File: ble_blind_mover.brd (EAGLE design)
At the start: 160 x 100 mm, 52 parts, among them J1 105017-0001, Q1 DMG6968U-7, Q2 DMG6968U-7, U1 MIC5205-3.3YM5-TR, U2 YJ-14015, U3 VIPER012LS

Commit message: Brd routed, clearance adjustment still WIP
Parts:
- removed C12: 470pF, rcl:C0603
- removed C15: 100uF, resistor:CT7343
- removed S1, S2: (no value), switch-omron:B3F-31XX
- removed U1: MIC5205-3.3YM5-TR, LTC_By_element14_Batch_1:SOT95P280X145-5N
- added C16, C17: 1uF, rcl:C0603
- added C18: 470pF, rcl:C0603
- added D6: STTH1L06A, xCommonLib:DO214AC
- added J2: (no value), tag-connect:TC2030-MCP-NL
- added R15: 0, rcl:0207/7
- added U4: MIC5205-3.3YM5-TR, LTC_By_element14_Batch_1:SOT95P280X145-5N
- C11: value 1uF -> 100uF; device rcl:C0603 -> rcl:C1812
- R9: device rcl:R0603 -> rcl:R1206
- moved S4 155.7 mm to (45.0, 55.0)
- moved S3 154.6 mm to (54.1, 55.0), turned to 90 degrees
- moved R11 142.7 mm to (53.6, 21.6), turned to 270 degrees
- moved C11 134.8 mm to (31.2, 10.7), turned to 90 degrees
- moved R9 129.3 mm to (34.3, 10.7), turned to 270 degrees
- moved R13 124.1 mm to (51.6, 21.6), turned to 90 degrees
- moved J1 117.3 mm to (10.9, 1.52)
- moved C10 109.8 mm to (24.6, 1.78), turned to 180 degrees
- moved C3 102.0 mm to (11.7, 48.0), turned to 90 degrees
- moved C1 99.0 mm to (7.62, 48.0), turned to 90 degrees
- moved SWD 97.5 mm to (34.3, 47.5)
- moved D2 91.2 mm to (36.8, 56.1), turned to 270 degrees
- moved R12 85.0 mm to (32.8, 57.1), turned to 180 degrees
- moved R4 79.6 mm to (5.59, 48.0), turned to 270 degrees
- moved R10 79.5 mm to (32.8, 59.2), turned to 180 degrees
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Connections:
- removed net N$11: C12.1, U1.4
- removed net VIPER_GND: C13.2, C7.2, D3.C, L1.1, U3.1, U3.3
- new net +5V: C10.1, C11.1, C16.1, D4.A, D6.C, L1.2, R9.2, U4.1, U4.3
- new net HOT_GND: C13.2, C14.2, C4.2, C5.2, C6.2, C7.2, D3.C, L1.1, R13.1, R15.2, U3.1, U3.3
- new net N$1: C18.1, U4.4
- net +3V3: now also C17.1, J2.1, U4.5; no longer C11.1, C15.+, D4.A, L1.2, R9.2, U1.5
- net BTN_DOWN: now also S4.1, S4.2; no longer S1.2
- net BTN_UP: no longer S2.2
- net GND: now also C16.2, C17.2, C18.2, J2.5, R15.1, U4.2; no longer C11.2, C12.2, S1.1, S2.1, U1.2
- net LED_B: now also U2.P.18; no longer U2.P.19
- net LED_G: now also U2.P.19; no longer U2.P.18
- net NEUTRAL: now also C11.2; no longer C14.2, C15.-, C4.2, C5.2, C6.2, R13.1
- net SWDCLK: now also J2.4
- net SWDIO: now also J2.2
- net VUSB: now also D6.A; no longer C10.1, U1.1, U1.3
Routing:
- net GND: track 0.00 -> 212.9 mm, vias 0 -> 4
- net +3V3: track 6.14 -> 146.5 mm, vias 0 -> 2
- net HOT_GND: track 0.00 -> 60.3 mm
- net +5V: track 0.00 -> 56.1 mm
- net BTN_UP: track 0.00 -> 41.0 mm, vias 0 -> 2
- net GO_DOWN: track 0.00 -> 32.0 mm
- net RELAY_COIL_UP: track 0.00 -> 31.9 mm, vias 0 -> 3
- net BTN_DOWN: track 0.00 -> 28.1 mm, vias 0 -> 1
- net NEUTRAL: track 96.6 -> 123.9 mm
- net GO_UP: track 0.00 -> 22.6 mm, vias 0 -> 2
- net VIPER_FB: track 1.97 -> 21.2 mm
- net LINE_FILTERED: track 10.9 -> 27.5 mm, vias 0 -> 1
- net VIPER_GND: track 16.4 -> 0.00 mm
- net SWDIO: track 0.00 -> 15.3 mm, vias 0 -> 1
- net SWDCLK: track 0.00 -> 15.0 mm, vias 0 -> 1
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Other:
- board size 160 x 100 mm -> 62 x 60.5 mm

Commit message: Fixed board eouting for increased low/high voltage clearance
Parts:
- removed R15: 0, rcl:0207/7
- added R16: 0, rcl:0207/7
- moved R9 4.74 mm to (35.8, 6.17)
- moved C11 4.74 mm to (32.7, 6.17)
- moved D3 4.51 mm to (32.7, 12.5)
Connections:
- removed net HOT_GND: C13.2, C14.2, C4.2, C5.2, C6.2, C7.2, D3.C, L1.1, R13.1, R15.2, U3.1, U3.3
- new net NEUTRAL_DISCONNECTABLE: C11.2, D3.A, R16.2, R9.1
- net GND: now also C13.2, C14.2, C4.2, C5.2, C6.2, C7.2, D3.C, L1.1, R13.1, U3.1, U3.3; no longer R15.1
- net NEUTRAL: now also R16.1; no longer C11.2, D3.A, R9.1
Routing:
- net HOT_GND: track 60.3 -> 0.00 mm
- net GND: track 212.9 -> 270.3 mm, vias 4 -> 5
- net NEUTRAL: track 123.9 -> 95.2 mm
- net NEUTRAL_DISCONNECTABLE: track 0.00 -> 24.2 mm
- net LINE_FILTERED: track 27.5 -> 32.1 mm
- net +5V: track 56.1 -> 54.5 mm
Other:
- outline, holes or cut-outs redrawn

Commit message: Added power connecting pinheads
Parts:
- added JP1, JP2: (no value), pinhead:1X02
- moved FUSE_MAINS 2.00 mm to (47.2, 35.8)
- moved D4 1.58 mm to (55.1, 15.0)
- moved D5 1.58 mm to (50.3, 15.0)
- moved C14 1.58 mm to (44.5, 17.0)
- moved C4 1.58 mm to (51.6, 17.6)
- moved C5 1.58 mm to (47.0, 18.3)
- moved C6 1.58 mm to (49.0, 18.3)
- moved L1 1.58 mm to (44.0, 6.88)
- moved R11 1.58 mm to (53.1, 20.1)
- moved R13 1.58 mm to (51.1, 20.1)
- moved R14 1.58 mm to (47.8, 20.9)
- moved C13 1.58 mm to (44.0, 14.5)
- moved C7 1.58 mm to (46.0, 14.5)
- moved U3 1.58 mm to (39.1, 15.8)
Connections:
- net NEUTRAL_DISCONNECTABLE renamed NEUTRAL_SEP
- net +3V3: now also JP1.1
- net +5V: now also JP2.1
- net GND: now also JP1.2, JP2.2
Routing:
- net +5V: track 54.5 -> 66.6 mm, vias 0 -> 2
- net LINE_UNFUSED: track 15.9 -> 13.9 mm
- net NEUTRAL_SEP: track 24.2 -> 22.5 mm
- net GND: track 270.3 -> 269.0 mm
- net LINE_FILTERED: track 32.1 -> 32.8 mm
- net NEUTRAL: track 95.2 -> 94.5 mm

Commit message: Aligned silkscreen labels
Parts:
- C1: value 10nF -> 10n
- C13, C2, C4: value 100nF -> 100n
- C18: value 470pF -> 470p
- C5: value 750pF -> 750p
- C6: value 22nF -> 22n
- C8, C9: value 120nF -> 120n
- L2: value 470uH -> 470u
- R1: value 15 -> 15R
- R10, R12, R8: value 470 -> 470R
- R16: value 0 -> 0R
- R3, R5: value 10 -> 10R
- renumbered D2 to LED1
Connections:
- net N$1 renamed U4_BYPASS
- new net SCL: U2.P.10
- new net SDA: U2.P.13
- net GO_UP: now also U2.P.12; no longer U2.P.13
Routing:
- net GO_DOWN: track 32.0 -> 31.1 mm
- net GO_UP: track 22.6 -> 23.5 mm

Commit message: Added RTC
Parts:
- added C12: 10n, rcl:C0603
- added C15: 100n, rcl:C0603
- added C19: 1uF, rcl:C0603
- added JP3: (no value), pinhead:1X02
- added R15, R17: 4K7, rcl:R0603
- added U1: MCP7940N-I/SN, MCP7940N-I_SN:SOIC127P600X175-8N
- added Y1: LFXTAL016178, LFXTAL016178:LFXTAL016178_1
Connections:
- new net RTC_XTAL1: U1.1, Y1.1
- new net RTC_XTAL2: U1.2, Y1.4
- new net VBAT: JP3.1, U1.3
- net +3V3: now also C12.1, C15.1, C19.1, R15.2, R17.2, U1.8
- net GND: now also C12.2, C15.2, C19.2, JP3.2, U1.4
- net SCL: now also R17.1, U1.6
- net SDA: now also R15.1, U1.5
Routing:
- net SCL: track 0.00 -> 23.5 mm, vias 0 -> 1
- net +3V3: track 146.9 -> 170.3 mm, vias 2 -> 3
- net SDA: track 0.00 -> 21.4 mm, vias 0 -> 1
- net GND: track 268.9 -> 282.3 mm
- net GO_DOWN: track 31.1 -> 42.1 mm
- net VBAT: track 0.00 -> 8.48 mm
- net RTC_XTAL2: track 0.00 -> 6.10 mm
- net BTN_DOWN: track 28.1 -> 25.1 mm
- net BTN_UP: track 41.0 -> 38.0 mm
- net RTC_XTAL1: track 0.00 -> 2.27 mm

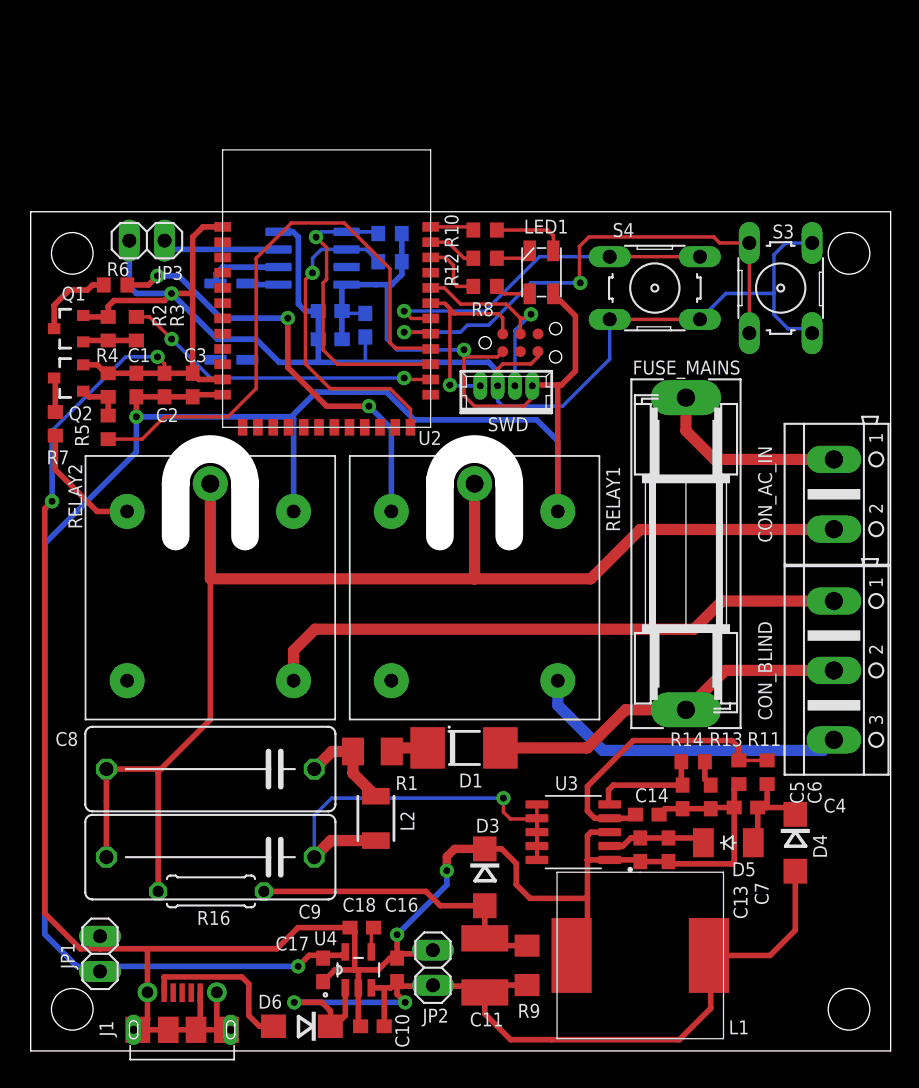
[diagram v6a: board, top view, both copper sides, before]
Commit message: - Get rid from Viper PSU in favour of a Meanwell module - Make the contours to fit in a Kradex Z21 box
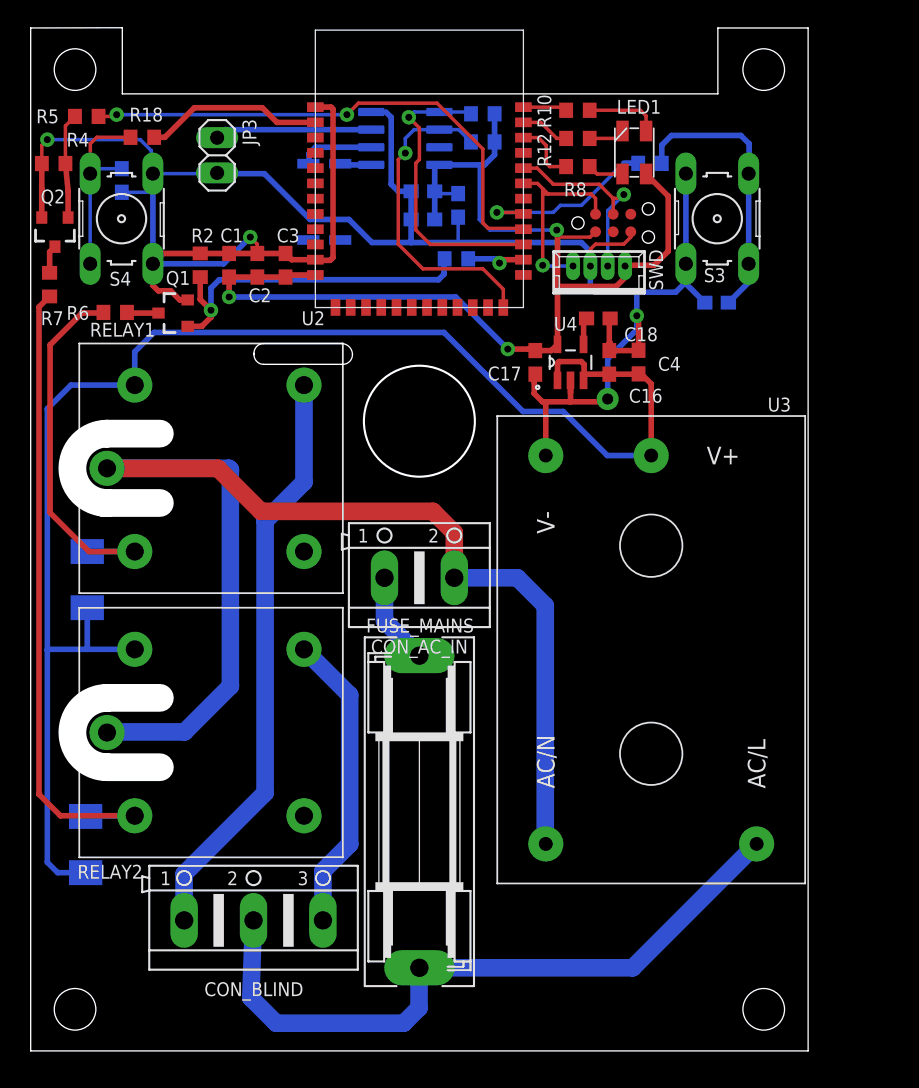
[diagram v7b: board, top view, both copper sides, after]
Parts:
- removed C10, C7: 1uF, rcl:C0603
- removed C11: 100uF, rcl:C1812
- removed C13: 100n, rcl:C0603
- removed C14: TBD, rcl:C0603
- removed C5: 750p, rcl:C0603
- removed C6: 22n, rcl:C0603
- removed C8, C9: 120n, rcl:C150-064X183
- removed D1: SM4007, _hhn_diodes_smd:MELF-MLL41_DO213AB
- removed D3, D4, D6: STTH1L06A, xCommonLib:DO214AC
- removed D5: (no value), diode_:SOD-123_MINI-SMA
- removed J1: 105017-0001, 105017-0001:MOLEX_105017-0001
- removed JP1, JP2: (no value), pinhead:1X02
- removed L1: DE1207-820, ferrocore:DE1207
- removed L2: 470u, SparkFun:1210
- removed R1: 15R, rcl:M1206
- removed R11: 82K, rcl:R0603
- removed R13: 47K, rcl:R0603
- removed R14: 100K, rcl:R0603
- removed R16: 0R, rcl:0207/7
- removed R9: 3K3, rcl:R1206
- added C20, C21: 10n, rcl:C0603
- added D2, D8: SK16, diode:DO-214AC
- added R18, R19: TBD, rcl:R0603
- RELAY1: value RM50-3011-85-1003 -> RM513021851005
- RELAY2: value RM50-3011-85-1003 -> RM51-3021-85-1005
- U3: value VIPER012LS -> IRM-01-5; device st_viper:SOIC100P600X175-10N -> meanwell_irm_v7:IRM_01/02
- moved C18 47.1 mm to (40.9, 52.8), turned to 0 degrees
- moved C16 46.4 mm to (41.7, 49.6)
- moved C17 46.4 mm to (36.4, 49.6)
- moved U4 46.4 mm to (38.9, 49.6)
- moved CON_BLIND 45.6 mm to (16.1, 9.41), turned to 0 degrees
- moved S4 38.8 mm to (6.55, 60.0), turned to 90 degrees
- moved C4 33.0 mm to (43.8, 49.7), turned to 90 degrees
- moved CON_AC_IN 30.5 mm to (28.0, 34.1), turned to 0 degrees
- moved FUSE_MAINS 26.7 mm to (28.0, 17.2)
- moved RELAY1 26.5 mm to (5.51, 42.0), turned to 0 degrees
- moved R3 23.6 mm to (30.7, 57.1), flipped to the bottom, turned to 0 degrees
- moved R5 22.5 mm to (4.04, 67.4), turned to 0 degrees
- moved RELAY2 19.4 mm to (5.51, 23.0), turned to 0 degrees
- moved R4 16.4 mm to (1.66, 64.0), turned to 0 degrees
- moved U3 14.3 mm to (44.7, 28.9), turned to 90 degrees
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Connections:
- removed net BLIND_DOWN: CON_BLIND.1, RELAY2.14
- removed net BLIND_UP: CON_BLIND.3, RELAY1.14
- removed net LINE_FILTERED: C9.1, L2.2, U3.10, U3.6, U3.7, U3.8, U3.9
- removed net LINE_RECTIFIED: D1.C, R1.1
- removed net LINE_RECTIFIED_R: C8.1, L2.1, R1.2
- removed net NEUTRAL_SEP: C11.2, D3.A, R16.2, R9.1
- removed net VIPER_COMP: C5.1, R14.2, U3.5
- removed net VIPER_COMP_MID: C6.1, R14.1
- removed net VIPER_FB: C14.1, R11.1, R13.2, U3.4
- removed net VIPER_PRE_FB: C4.1, D4.C, D5.A, R11.2
- removed net VIPER_VCC: C13.1, C7.1, D5.C, U3.2
- removed net VUSB: D6.A, J1.1
- new net BLIND_DOWN_AC: CON_BLIND.3, RELAY2.14
- new net BLIND_UP_AC: CON_BLIND.1, RELAY1.14
- new net BTN_DOWN_R: C20.1, R18.1, S4.1, S4.2
- new net BTN_UP_R: C21.1, R19.1, S3.1, S3.2
- net +3V3: no longer JP1.1, RELAY1.A1, RELAY2.A1
- net +5V: now also C4.1, D2.C, D8.C, RELAY1.A1, RELAY2.A1, U3.V+; no longer C10.1, C11.1, D4.A, D6.C, JP2.1, L1.2, R9.2
- net BTN_DOWN: now also R18.2, U2.P.21; no longer S4.1, S4.2, U2.P.16
- net BTN_UP: now also R19.2; no longer S3.1, S3.2
- net GND: now also C20.2, C21.2, U3.V-; no longer C10.2, C13.2, C14.2, C5.2, C6.2, C7.2, D3.C, J1.5, J1.MH1, J1.MH2, J1.MH3, J1.MH4, J1.P$10, J1.P$11, J1.P$8, J1.P$9, JP1.2, JP2.2, L1.1, R13.1, U3.1, U3.3
- net LINE_FUSED: now also U3.AC/L; no longer D1.A
- net NEUTRAL: now also U3.AC/N; no longer C8.2, C9.2, R16.1
- net RELAY_COIL_DOWN: now also D8.A
- net RELAY_COIL_UP: now also D2.A
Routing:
- net GND: track 282.3 -> 166.7 mm, vias 5 -> 4
- net +3V3: track 170.3 -> 86.6 mm
- net +5V: track 66.6 -> 111.0 mm, vias 2 -> 0
- net BLIND_DOWN: track 42.6 -> 0.00 mm
- net BLIND_UP_AC: track 0.00 -> 42.2 mm
- net RELAY_COIL_DOWN: track 8.88 -> 47.3 mm
- net LINE_FILTERED: track 32.8 -> 0.00 mm, vias 1 -> 0
- net BTN_UP: track 38.0 -> 13.6 mm, vias 2 -> 1
- net LINE_FUSED: track 26.4 -> 49.8 mm
- net BLIND_UP: track 23.3 -> 0.00 mm
- net NEUTRAL_SEP: track 22.5 -> 0.00 mm
- net BLIND_DOWN_AC: track 0.00 -> 21.7 mm
- net MOTOR_A_GATE_R: track 3.87 -> 25.1 mm, vias 0 -> 1
- net VIPER_FB: track 21.2 -> 0.00 mm
- net BTN_UP_R: track 0.00 -> 20.3 mm
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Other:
- board size 62 x 60.5 mm -> 56 x 73.8 mm

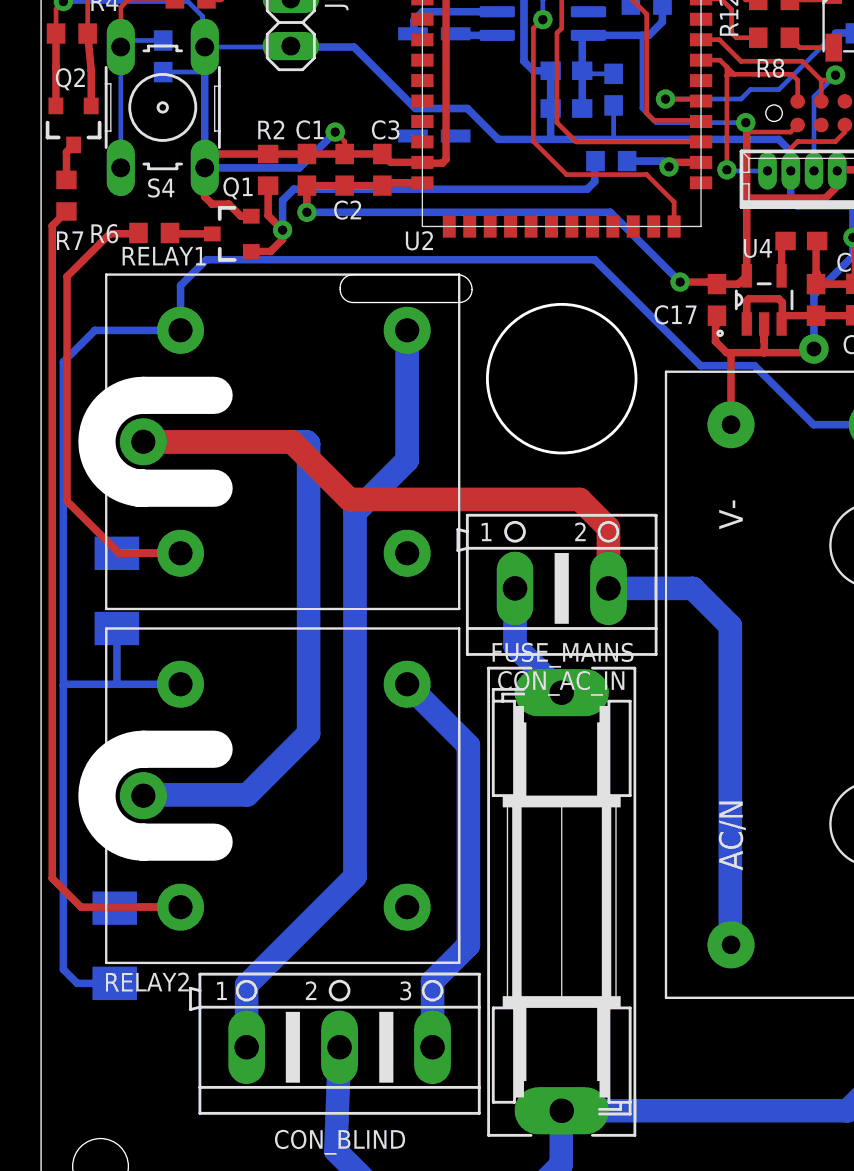
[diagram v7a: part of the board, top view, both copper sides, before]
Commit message: MOved to a triac based design
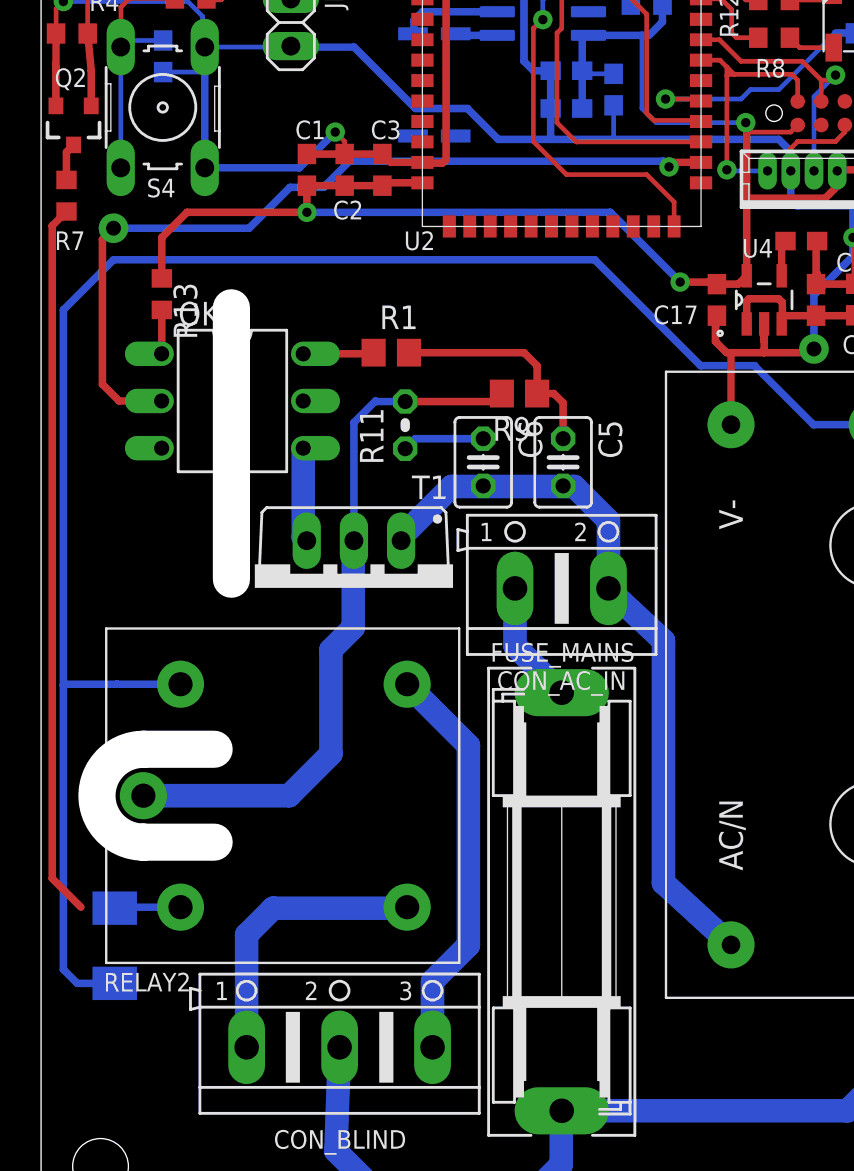
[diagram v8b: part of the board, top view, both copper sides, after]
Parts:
- removed D2: SK16, diode:DO-214AC
- removed Q1: DMG6968U-7, SparkFun:SOT23-3
- removed R2: 47K, rcl:R0603
- removed R3: 10R, rcl:R0603
- removed R6: TBD, rcl:R0603
- removed RELAY1: RM513021851005, relay-relpol:RM50-3011-XX-XXXX
- added C5: 47nF, rcl:C025-030X050
- added C6: 10nF, rcl:C025-030X050
- added OK1: MOC3023M, optocoupler:DIL06
- added R1: 360, rcl:R0805
- added R11: 39, rcl:0204V
- added R13: 360, rcl:R0603
- added R9: 470, rcl:R0805
- added T1: BT138-V, triac:TO220BV
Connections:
- net GO_DOWN renamed DIRECTION
- net RELAY_COIL_DOWN renamed RELAY_COIL_DIR
- net RELAY_COIL_DOWN__R renamed RELAY_COIL_DIR_R
- removed net GO_UP: R3.1, U2.P.12
- removed net MOTOR_A_GATE_R: Q1.1, R2.1, R3.2
- removed net RELAY_COIL_UP: D2.A, R6.2, RELAY1.A2
- removed net RELAY_COIL_UP__R: Q1.3, R6.1
- new net ENABLE: OK1.2, U2.P.12
- new net LOAD_B: R11.2, R9.2, RELAY2.11, T1.T2
- new net MOC_AN: OK1.1, R13.2
- new net MOC_OUT: OK1.6, R1.1
- new net N$2: C5.1, R1.2, R9.1
- new net SNUB_MID: C6.1, R11.1
- new net TRIAC_GET: OK1.4, T1.G
- net +3V3: now also R13.1
- net +5V: no longer D2.C, RELAY1.A1
- net BLIND_UP_AC: now also RELAY2.12; no longer RELAY1.14
- net GND: no longer Q1.2, R2.2
- net NEUTRAL: now also C5.2, C6.2, T1.T1; no longer RELAY1.11, RELAY2.11
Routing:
- net NEUTRAL: track 89.6 -> 40.0 mm
- net ENABLE: track 0.00 -> 45.6 mm, vias 0 -> 2
- net LOAD_B: track 0.00 -> 38.0 mm
- net RELAY_COIL_UP: track 27.6 -> 0.00 mm
- net BLIND_UP_AC: track 42.2 -> 15.3 mm
- net MOTOR_A_GATE_R: track 25.1 -> 0.00 mm, vias 1 -> 0
- net N$2: track 0.00 -> 12.2 mm
- net +3V3: track 86.6 -> 97.2 mm
- net GND: track 166.7 -> 156.3 mm
- net RELAY_COIL_DIR: track 47.3 -> 42.0 mm
- net TRIAC_GET: track 0.00 -> 5.06 mm
- net SNUB_MID: track 0.00 -> 4.42 mm
- net GO_UP: track 4.21 -> 0.00 mm, vias 1 -> 0
- net MOC_OUT: track 0.00 -> 3.81 mm
- net +5V: track 111.0 -> 108.3 mm
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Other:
- outline, holes or cut-outs redrawn
